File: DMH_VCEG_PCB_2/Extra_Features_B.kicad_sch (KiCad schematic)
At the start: 50 parts, among them J25 Conn_01x10_PinHeader, J26 Conn_01x10_PinHeader, Q8 BC548, SW2 SW_DPDT_x2, SW5 SW_DPDT_x2_On-Off-(On), U10 TL074, U12 40106, U17 TL074, U20 4001

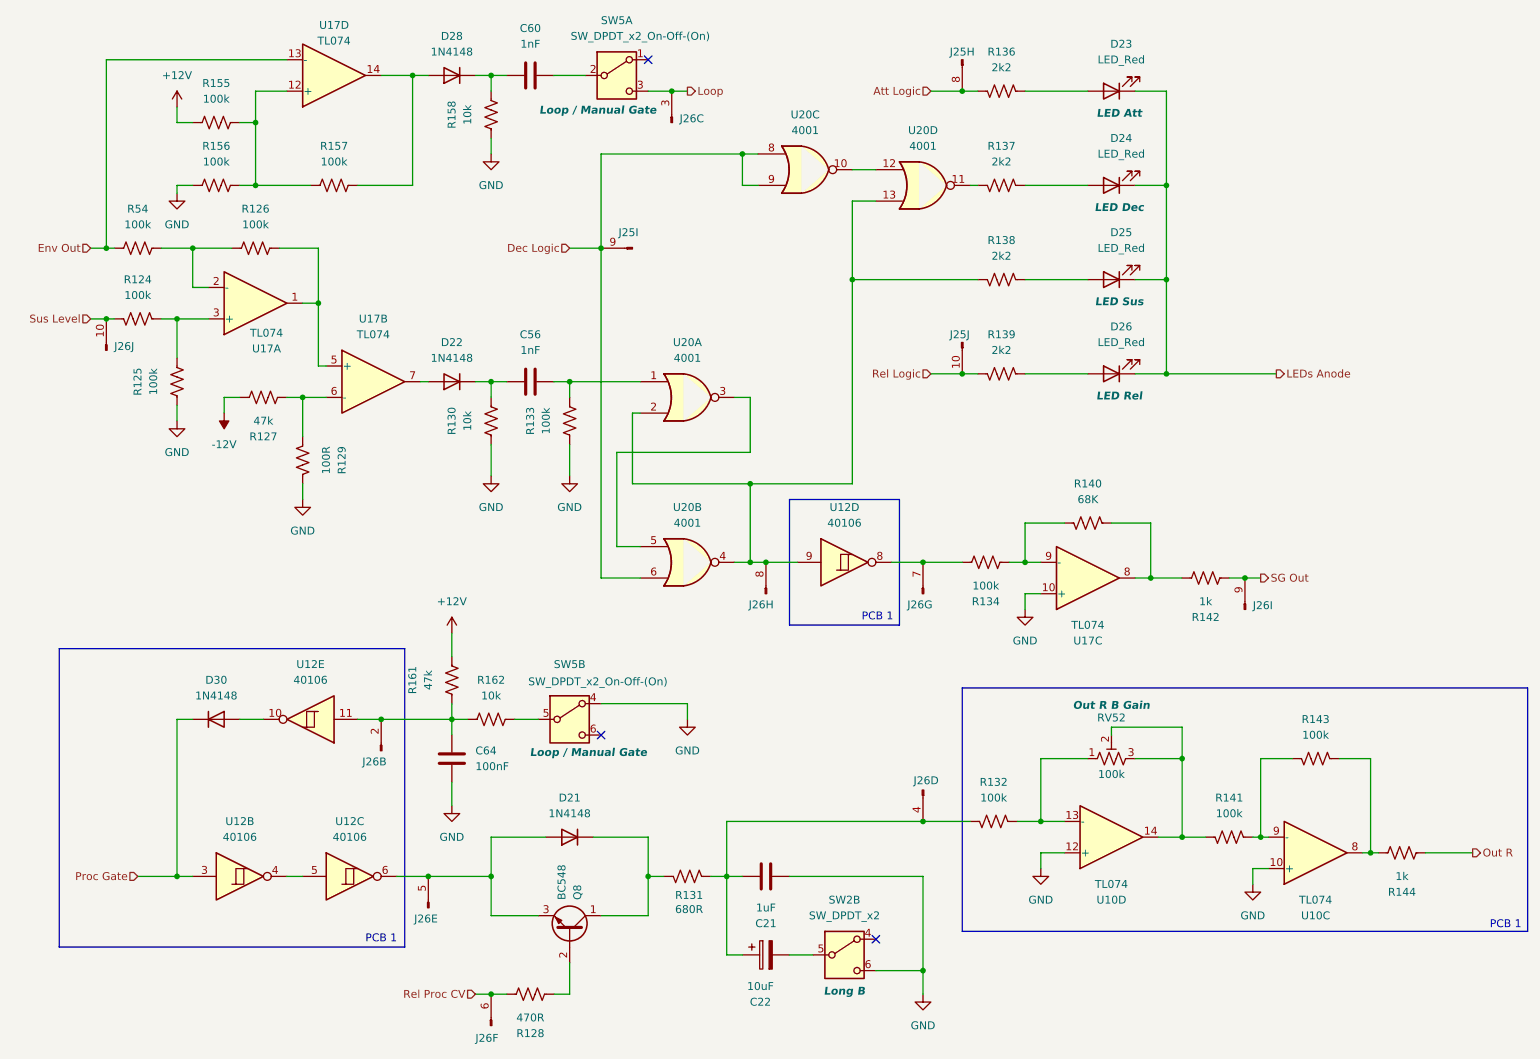
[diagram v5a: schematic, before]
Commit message: Synced PCB 2 project with PCB 1
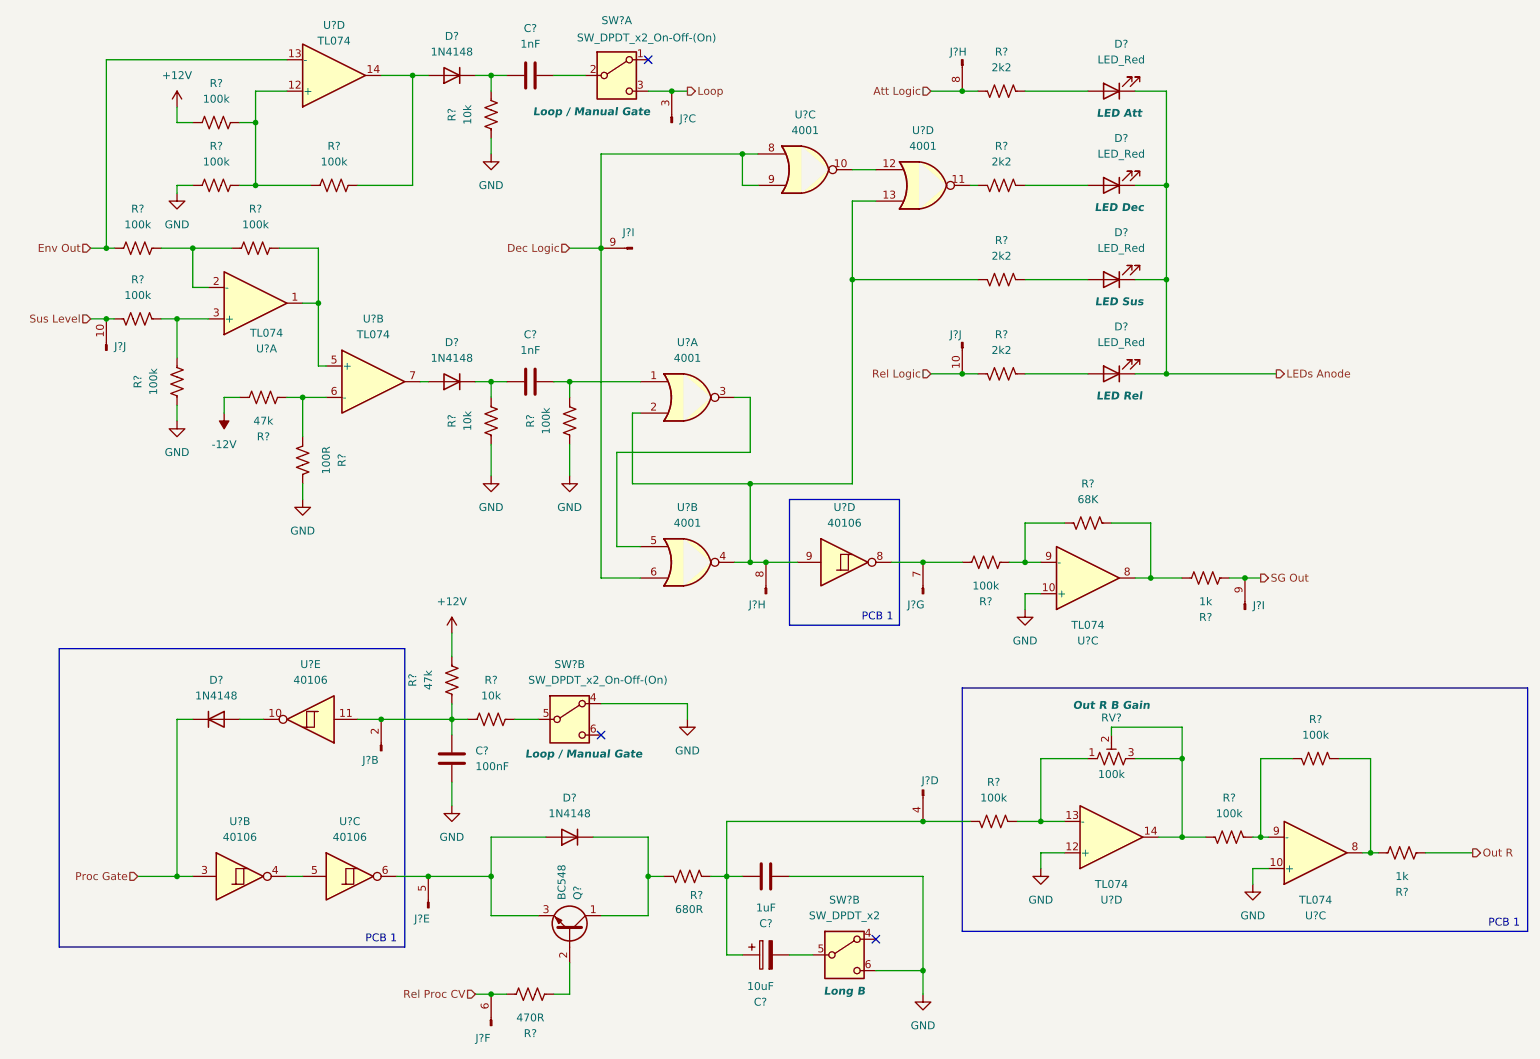
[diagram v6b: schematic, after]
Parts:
- removed D30: 1N4148, Diode_THT:D_DO-35_SOD27_P7.62mm_Horizontal, symbol Diode:1N4148
- removed unit 2 of J26
- removed unit 4 of J26
- removed SW5: SW_DPDT_x2_On-Off-(On), SynthStuff:Toggle_Switch_2_Poles_TE, symbol Switch:SW_DPDT_x2
- removed unit 5 of U12
- added D?: 1N4148, Diode_THT:D_DO-35_SOD27_P7.62mm_Horizontal, symbol Diode:1N4148
- added J?: Conn_01x10_PinHeader, symbol SynthStuff:Conn_01x10_PinHeader
- added J?: Conn_01x10_PinHeader, Connector_PinHeader_2.54mm:PinHeader_1x10_P2.54mm_Vertical, symbol SynthStuff:Conn_01x10_PinHeader
- added SW? (x2): SW_DPDT_x2_On-Off-(On), symbol Switch:SW_DPDT_x2
- added U?: 40106, Package_DIP:DIP-14_W7.62mm_Socket, symbol 4xxx:40106
- J? (x7): renamed from J26; footprint Connector_PinSocket_2.54mm:PinSocket_1x10_P2.54mm_Vertical -> (none)
- J? (x3): renamed from J25; footprint Connector_PinSocket_2.54mm:PinSocket_1x10_P2.54mm_Vertical -> (none)
- renumbered C21 to C?, C22 to C?, C60 to C?, C64 to C?, C56 to C?, D26 to D?, D28 to D?, D21 to D?, D23 to D?, D24 to D?, D25 to D?, D22 to D?, Q8 to Q?, R162 to R?, R143 to R?, R125 to R?, R136 to R?, R130 to R?, R157 to R?, R138 to R?, R158 to R?, R155 to R?, R129 to R?, R141 to R?, R126 to R?, R133 to R?, R54 to R?, R132 to R?, R134 to R?, R131 to R?, R161 to R?, R142 to R?, R128 to R?, R137 to R?, R156 to R?, R139 to R?, R124 to R?, R144 to R?, R127 to R?, R140 to R?, RV52 to RV?, SW2 to SW?, U17 to U?, U12 to U?, U20 to U?, U10 to U?
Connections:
- net GND: now also SW?.4 (A)
- net Loop: now also SW?.3 (C)
- net Proc Gate: now also D?.1 (K)
- net at C?.1, C?.1, R?.1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: now also J?.4 (Pin_4)
- net at R?.1: now also SW?.5 (B)
- net at C?.1, R?.2, R?.2: now also J?.2 (Pin_2), U?.11
- net at C?.2: now also SW?.2 (B)
- new net: D?.2 (A), U?.10
